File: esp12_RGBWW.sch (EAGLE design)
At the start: 36 parts, among them Q1 AOD2910SMD, Q2 AOD2910SMD, Q3 AOD2910SMD, Q4 AOD2910SMD, Q5 AOD2910SMD, U1 TPS5410DR

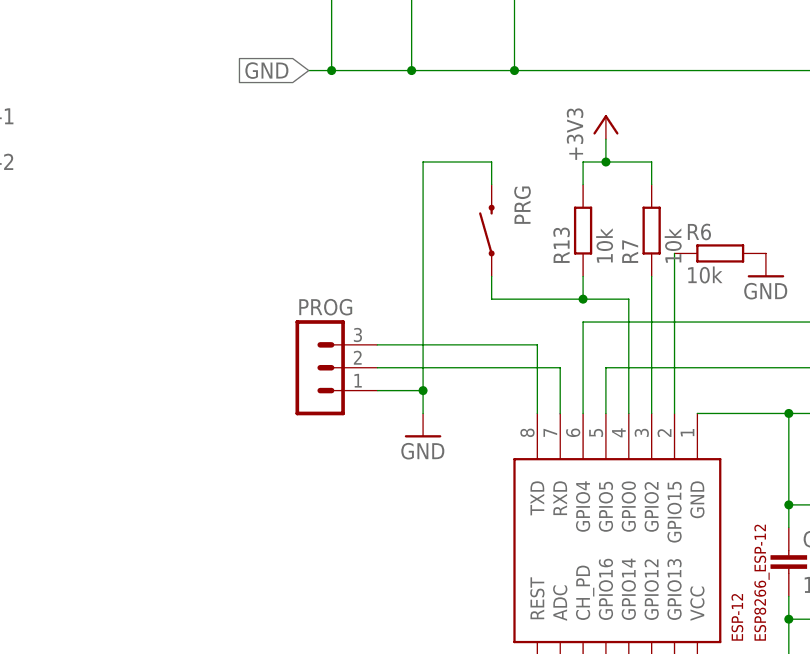
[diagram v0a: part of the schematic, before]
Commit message: added six pin connector for programming
changed the three pin programming header to a six pin version, allowing to directly plug in one of the universal FTDI based USB to UART adaptors.
Pinout is:
1: GND
2: NC
3: NC
4: RX
5: TX
6: NC

with RX and TX being from the ESP's point of view and Pin1 being on the far side from the ESP.

This is currently untested. There was some moving around of components on the DC/DC converter but I don't think that made for any substantial change
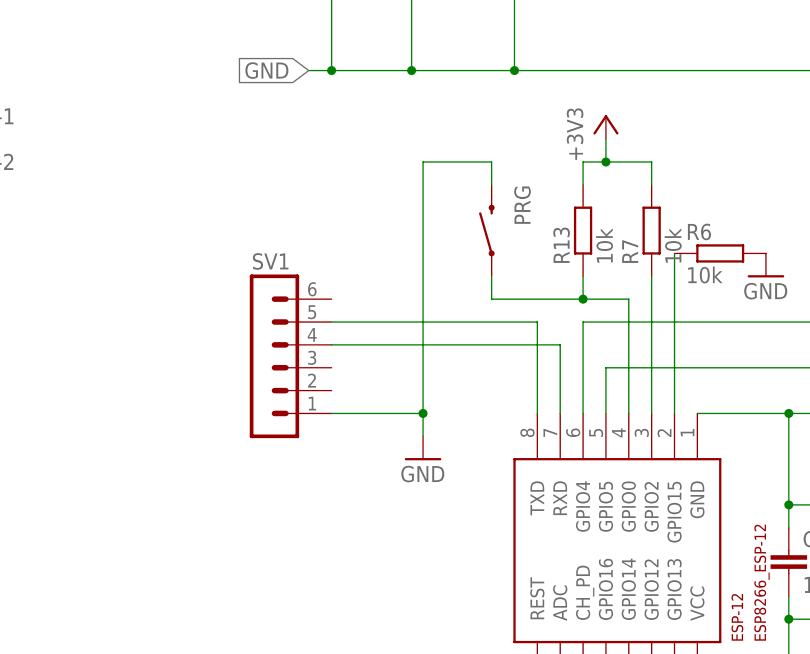
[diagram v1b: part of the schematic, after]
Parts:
- removed PROG: (no value), con-lstb:MA03-1
- added SV1: (no value), con-lstb:MA06-1
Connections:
- net GND: now also SV1.1; no longer PROG.1
- net RXD: now also SV1.4; no longer PROG.2
- net TXD: now also SV1.5; no longer PROG.3
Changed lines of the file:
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@@
 <part name="Q3" library="transistor-fet+irf7201" deviceset="AOD2910" device="" technology="SMD"/>
 <part name="C3" library="resistor" deviceset="CPOL-EU" device="E2.5-7" value="240uF"/>
-<part name="PROG" library="con-lstb" deviceset="MA03-1" device=""/>
 <part name="C5" library="rcl" deviceset="C-EU" device="C0805" value="10n"/>
 <part name="DISABLE" library="pinhead" deviceset="PINHD-1X2" device=""/>
+<part name="SV1" library="con-lstb" deviceset="MA06-1" device=""/>
 </parts>
 <sheets>
@@
 <instance part="GND12" gate="1" x="53.34" y="60.96"/>
 <instance part="+3V4" gate="G$1" x="22.86" y="-7.62"/>
-<instance part="GND13" gate="1" x="15.24" y="43.18"/>
+<instance part="GND13" gate="1" x="15.24" y="40.64"/>
 <instance part="R10" gate="G$1" x="27.94" y="5.08" rot="R90"/>
 <instance part="C2" gate="G$1" x="60.96" y="30.48"/>
@@
 <attribute name="VALUE" x="6.223" y="99.5426" size="1.778" layer="96"/>
 </instance>
-<instance part="PROG" gate="G$1" x="2.54" y="50.8"/>
 <instance part="C5" gate="G$1" x="55.88" y="30.48"/>
 <instance part="DISABLE" gate="G$1" x="2.54" y="139.7" rot="R180"/>
+<instance part="SV1" gate="1" x="-2.54" y="53.34"/>
 </instances>
 <busses>
@@
 <segment>
 <pinref part="GND13" gate="1" pin="GND"/>
-<wire x1="15.24" y1="45.72" x2="15.24" y2="48.26" width="0.1524" layer="91"/>
+<wire x1="15.24" y1="43.18" x2="15.24" y2="45.72" width="0.1524" layer="91"/>
 <pinref part="PRG" gate="G$1" pin="2"/>
-<wire x1="15.24" y1="48.26" x2="15.24" y2="73.66" width="0.1524" layer="91"/>
+<wire x1="15.24" y1="45.72" x2="15.24" y2="73.66" width="0.1524" layer="91"/>
 <wire x1="15.24" y1="73.66" x2="22.86" y2="73.66" width="0.1524" layer="91"/>
 <wire x1="22.86" y1="73.66" x2="22.86" y2="71.12" width="0.1524" layer="91"/>
-<pinref part="PROG" gate="G$1" pin="1"/>
-<wire x1="10.16" y1="48.26" x2="15.24" y2="48.26" width="0.1524" layer="91"/>
-<junction x="15.24" y="48.26"/>
+<junction x="15.24" y="45.72"/>
+<pinref part="SV1" gate="1" pin="1"/>
+<wire x1="5.08" y1="45.72" x2="15.24" y2="45.72" width="0.1524" layer="91"/>
 </segment>
 <segment>
@@
 <segment>
 <pinref part="ESP-12" gate="G$1" pin="RXD"/>
-<wire x1="30.48" y1="50.8" x2="30.48" y2="45.72" width="0.1524" layer="91"/>
-<pinref part="PROG" gate="G$1" pin="2"/>
-<wire x1="10.16" y1="50.8" x2="30.48" y2="50.8" width="0.1524" layer="91"/>
+<wire x1="30.48" y1="53.34" x2="30.48" y2="45.72" width="0.1524" layer="91"/>
+<pinref part="SV1" gate="1" pin="4"/>
+<wire x1="30.48" y1="53.34" x2="5.08" y2="53.34" width="0.1524" layer="91"/>
 </segment>
 </net>
@@
 <segment>
 <pinref part="ESP-12" gate="G$1" pin="TXD"/>
-<pinref part="PROG" gate="G$1" pin="3"/>
-<wire x1="10.16" y1="53.34" x2="27.94" y2="53.34" width="0.1524" layer="91"/>
-<wire x1="27.94" y1="53.34" x2="27.94" y2="45.72" width="0.1524" layer="91"/>
-</segment>
-</net>
+<wire x1="27.94" y1="55.88" x2="27.94" y2="45.72" width="0.1524" layer="91"/>
+<pinref part="SV1" gate="1" pin="5"/>
+<wire x1="27.94" y1="55.88" x2="5.08" y2="55.88" width="0.1524" layer="91"/>
+</segment>
+</net>

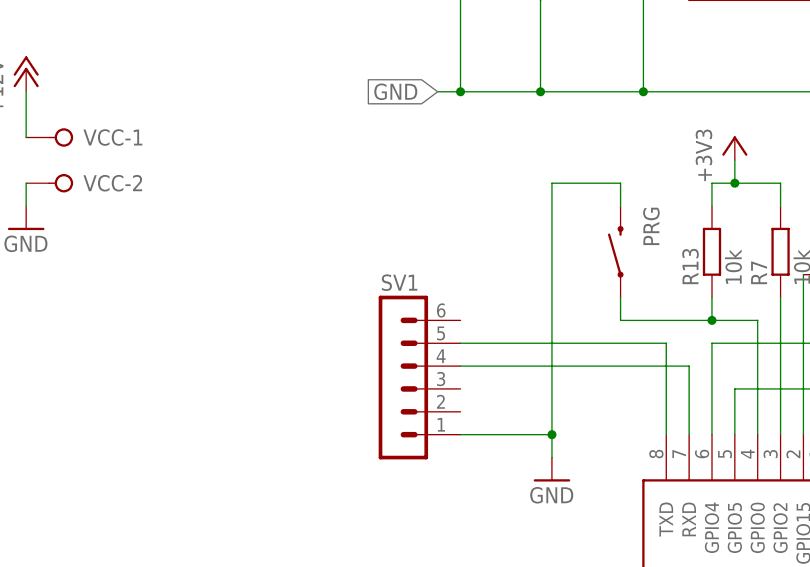
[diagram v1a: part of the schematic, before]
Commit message: created a bit more room for a sliding mount by moving the decoupling caps C2 and C5 in a bit.
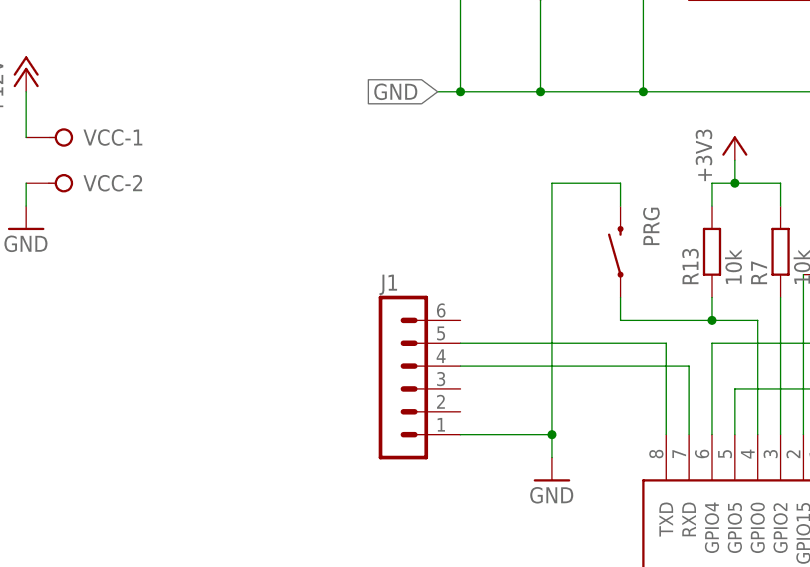
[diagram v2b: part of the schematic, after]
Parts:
- renumbered SV1 to J1
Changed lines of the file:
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@@
 <part name="C5" library="rcl" deviceset="C-EU" device="C0805" value="10n"/>
 <part name="DISABLE" library="pinhead" deviceset="PINHD-1X2" device=""/>
-<part name="SV1" library="con-lstb" deviceset="MA06-1" device=""/>
+<part name="J1" library="con-lstb" deviceset="MA06-1" device=""/>
 </parts>
 <sheets>
@@
 <instance part="C5" gate="G$1" x="55.88" y="30.48"/>
 <instance part="DISABLE" gate="G$1" x="2.54" y="139.7" rot="R180"/>
-<instance part="SV1" gate="1" x="-2.54" y="53.34"/>
+<instance part="J1" gate="1" x="-2.54" y="53.34"/>
 </instances>
 <busses>
@@
 <wire x1="22.86" y1="73.66" x2="22.86" y2="71.12" width="0.1524" layer="91"/>
 <junction x="15.24" y="45.72"/>
-<pinref part="SV1" gate="1" pin="1"/>
+<pinref part="J1" gate="1" pin="1"/>
 <wire x1="5.08" y1="45.72" x2="15.24" y2="45.72" width="0.1524" layer="91"/>
 </segment>
@@
 <pinref part="ESP-12" gate="G$1" pin="RXD"/>
 <wire x1="30.48" y1="53.34" x2="30.48" y2="45.72" width="0.1524" layer="91"/>
-<pinref part="SV1" gate="1" pin="4"/>
+<pinref part="J1" gate="1" pin="4"/>
 <wire x1="30.48" y1="53.34" x2="5.08" y2="53.34" width="0.1524" layer="91"/>
 </segment>
@@
 <pinref part="ESP-12" gate="G$1" pin="TXD"/>
 <wire x1="27.94" y1="55.88" x2="27.94" y2="45.72" width="0.1524" layer="91"/>
-<pinref part="SV1" gate="1" pin="5"/>
+<pinref part="J1" gate="1" pin="5"/>
 <wire x1="27.94" y1="55.88" x2="5.08" y2="55.88" width="0.1524" layer="91"/>
 </segment>
